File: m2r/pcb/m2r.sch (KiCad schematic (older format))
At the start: 105 parts, among them IC1 ADP3338, IC10 STM32F303C, IC11 TPS76327, IC2 APU1205-HF-3, IC3 ADuM1201, IC4 ADuM1201, IC5 SP100-2T, IC6 ADL5324, IC7 NTX2B, IC8 MAX-7Q, IC9 ALM-2712, P1 CONN_2, P2 CONN_4, P3 RockBLOCK, P4 SWD, P5 SMA, P6 CONN_2, X1 BAT BOX, X2 ARM SW, X3 RG LED, X4 8M

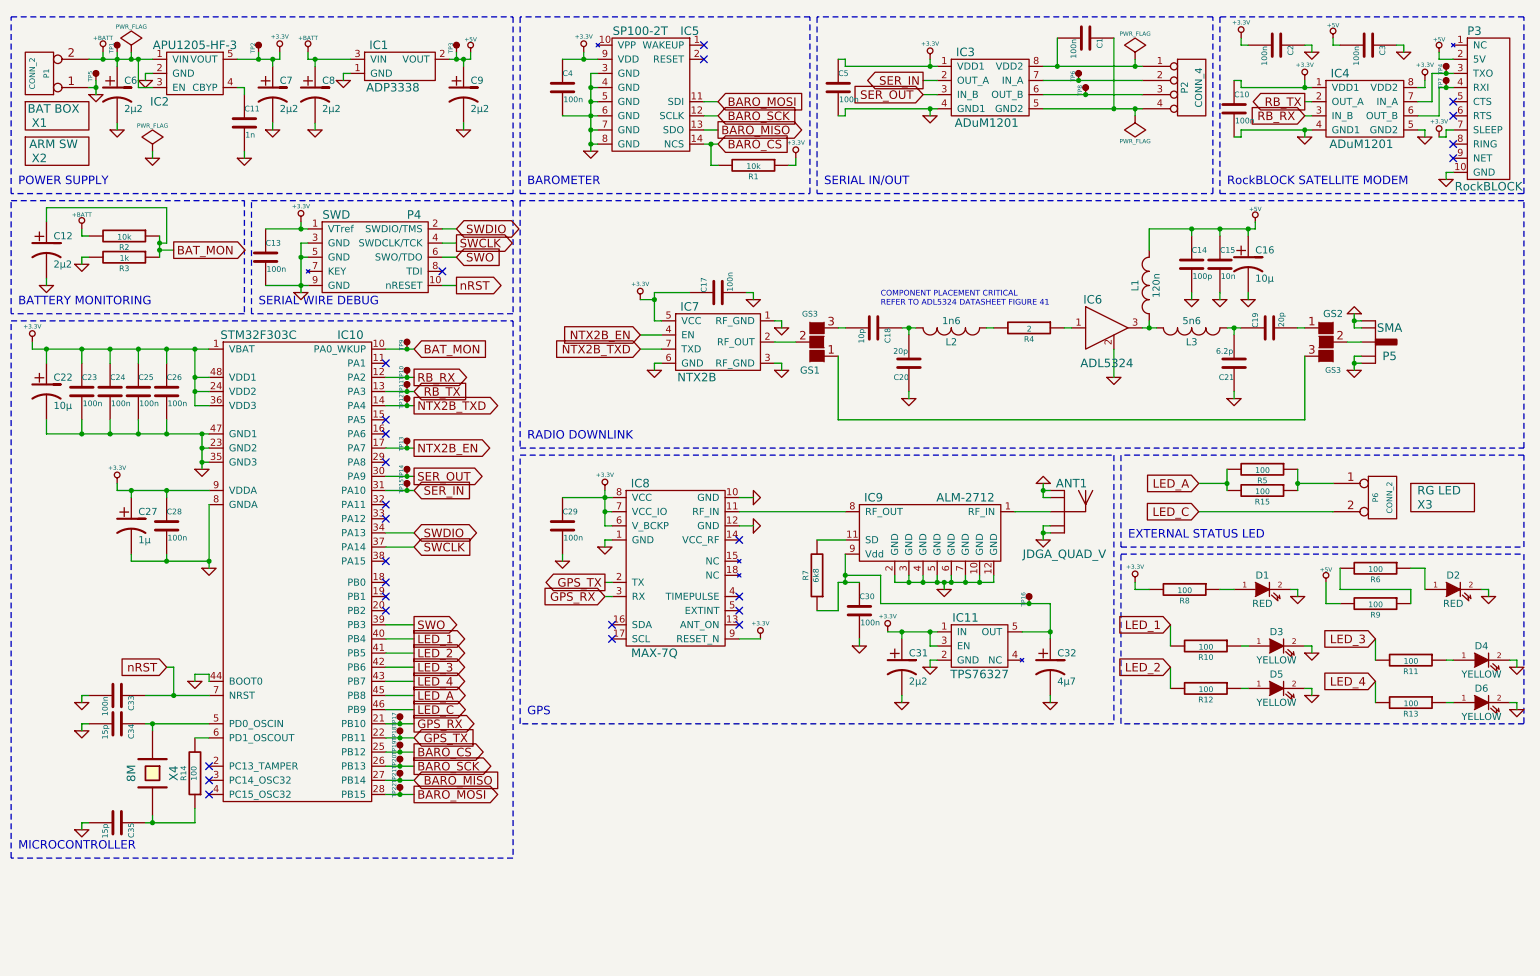
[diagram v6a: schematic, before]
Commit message: Add second connector for arming switch to m2r
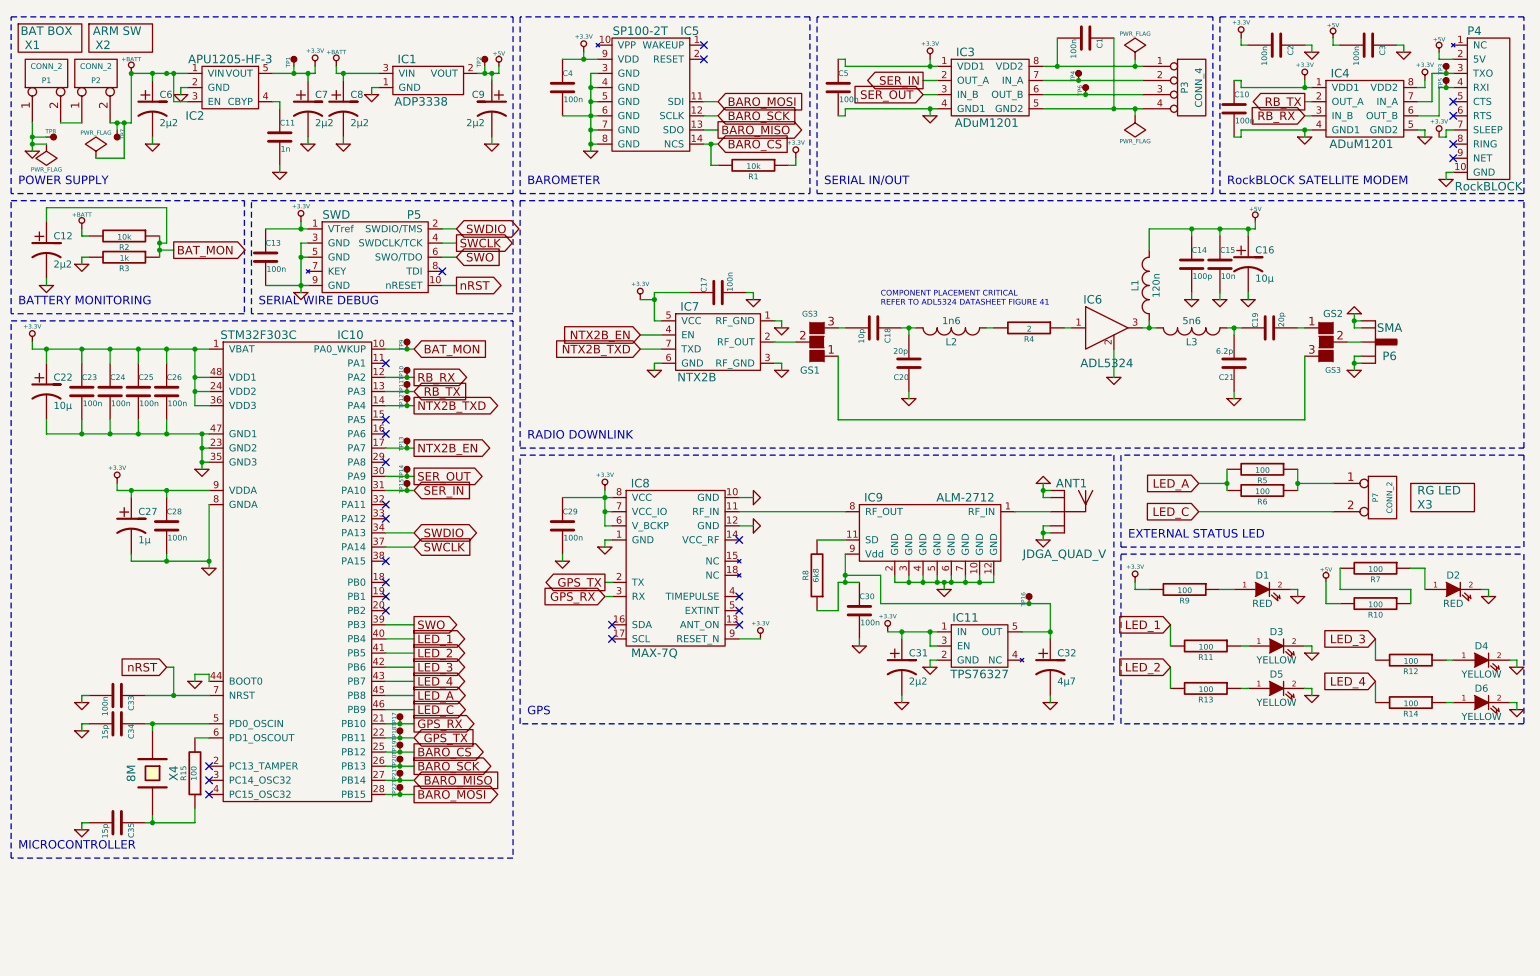
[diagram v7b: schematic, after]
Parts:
- added P2: CONN_2, symbol CONN_2
- renumbered P2 to P3, P3 to P4, P4 to P5, P5 to P6, P6 to P7, R9 to R10, R10 to R11, R11 to R12, R12 to R13, R13 to R14, R14 to R15, R15 to R6, R6 to R7, R7 to R8, R8 to R9, TP2 to TP1, TP3 to TP2, TP4 to TP3, TP6 to TP4, TP7 to TP5, TP8 to TP6, TP1 to TP7, TP5 to TP8
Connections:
- net +BATT: now also P2.2 (PM); no longer P1.2 (PM)
- new net: P1.2 (PM), P2.1 (P1)
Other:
- moved on the sheet: C11, C6, C7, C8, C9, IC1, IC2, P1, TP1, TP2, TP7, TP8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

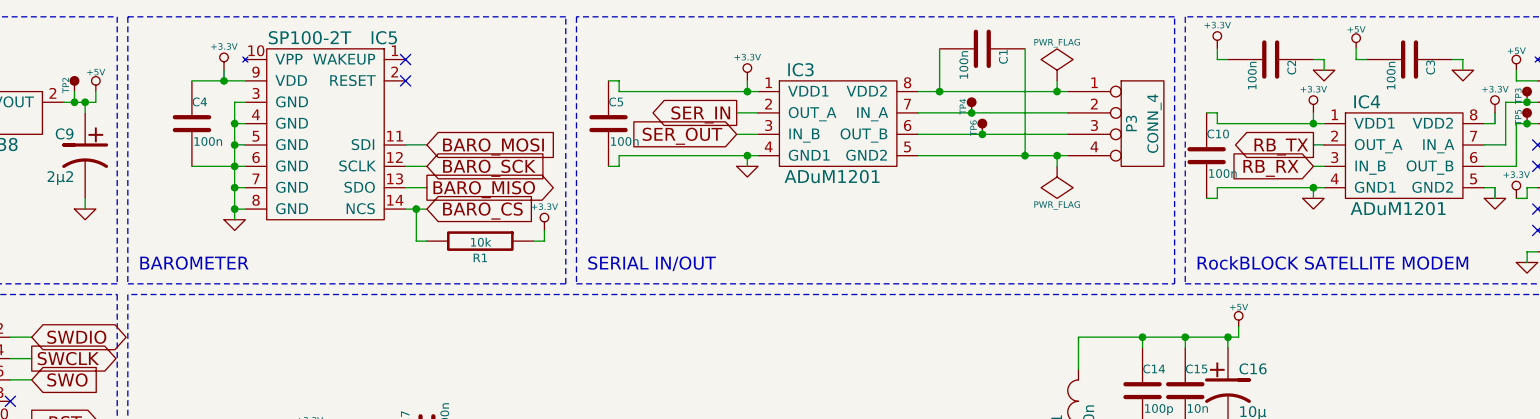
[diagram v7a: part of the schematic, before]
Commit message: swap SP100-2T for MS5611-01BA03 barometer
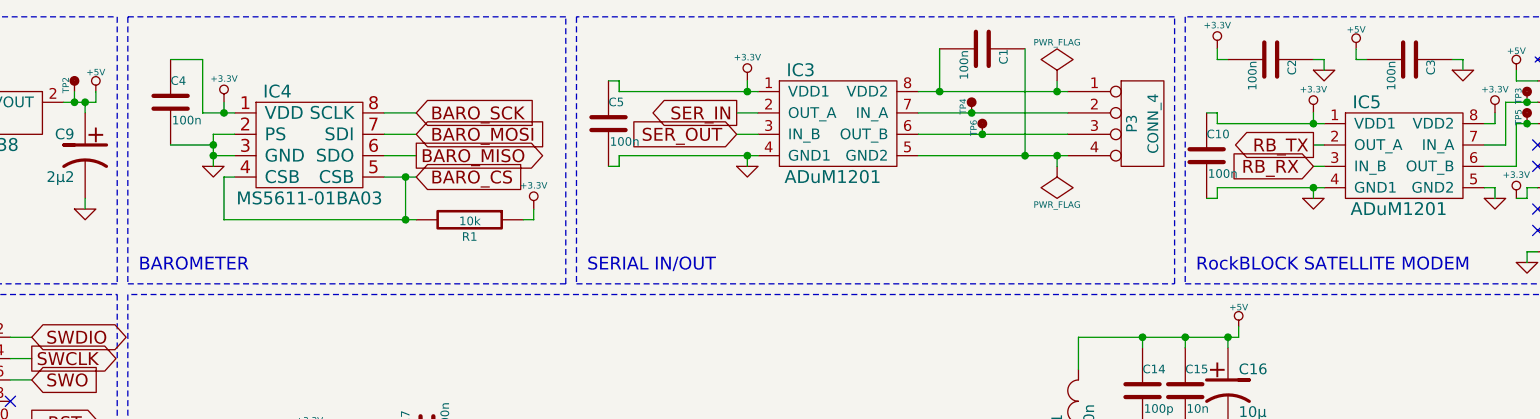
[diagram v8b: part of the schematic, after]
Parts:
- removed IC5: SP100-2T, symbol SP100-2T
- added IC4: MS5611-01BA03, symbol MS5611-01BA03
- renumbered IC4 to IC5
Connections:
- net +3.3V: now also IC4.1 (VDD)
- net BARO_CS: now also IC4.4 (CSB), IC4.5 (CSB)
- net BARO_MISO: now also IC4.6 (SDO)
- net BARO_MOSI: now also IC4.7 (SDI)
- net BARO_SCK: now also IC4.8 (SCLK)
- net GND: now also IC4.2 (PS), IC4.3 (GND)
- no-connect marks 26 -> 24
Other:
- moved on the sheet: C4, R1
